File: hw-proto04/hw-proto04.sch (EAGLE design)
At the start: 35 parts, among them IC1 VN5E160MSTR-E, IC2 UCC27523DR, IC3 MCP2562T, IC4 STM32F042C6T7, IC5 TLV74333PDBVR, J1 10, J2 10, Q1 SQJ147ELP-T1_GE3, Q2 SQJ147ELP-T1_GE3

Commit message: schematic refinements
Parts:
- removed SER: (no value), SparkFun-Connectors:M04LOCK
- added UART1: (no value), SparkFun-Connectors:M04LOCK
- IC4: value STM32F042C6T7 -> STM32F042
- IC5: value TLV74333PDBVR -> TLV74333P
- renumbered J1 to R3, J2 to R2, PRG to SWLINK
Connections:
- net +3V3: now also UART1.1; no longer SER.4
- net GND: now also SWLINK.2, UART1.2; no longer SER.1, SWLINK.4
- net RX1: now also UART1.4; no longer SER.3
- net SWCLK: now also SWLINK.4; no longer SWLINK.3
- net SWDIO: now also SWLINK.3; no longer SWLINK.2
- net TX1: now also UART1.3; no longer SER.2
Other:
- moved on the sheet: PWR

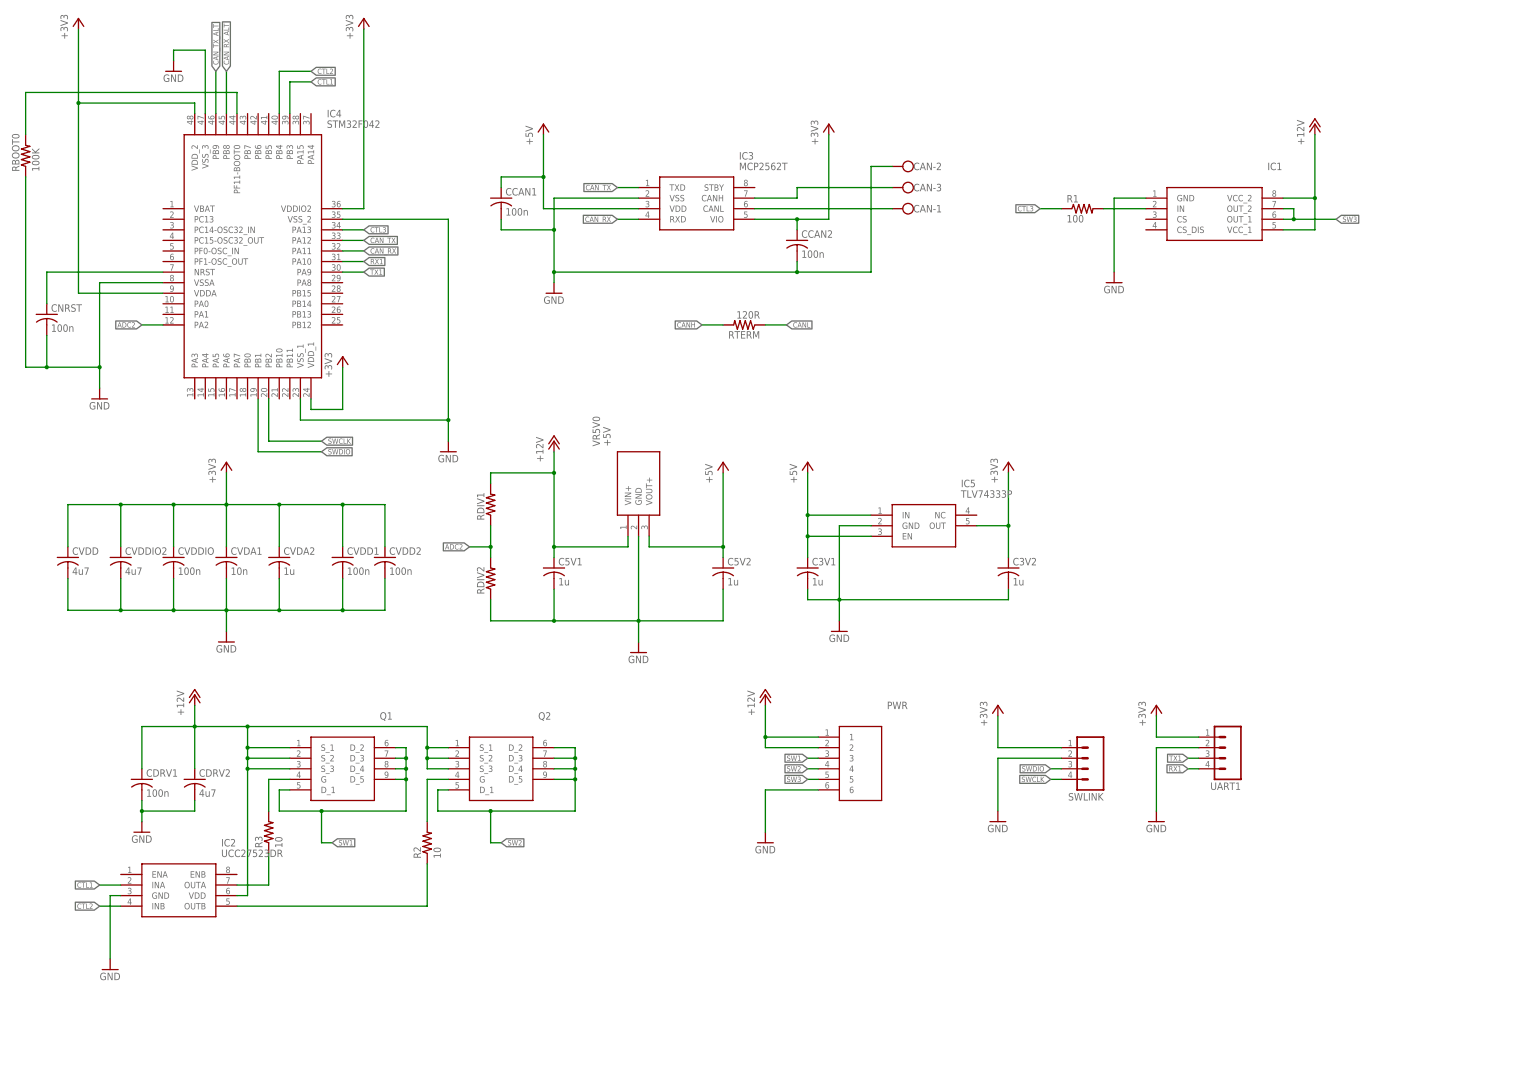
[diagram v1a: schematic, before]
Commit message: silkscreen refinement
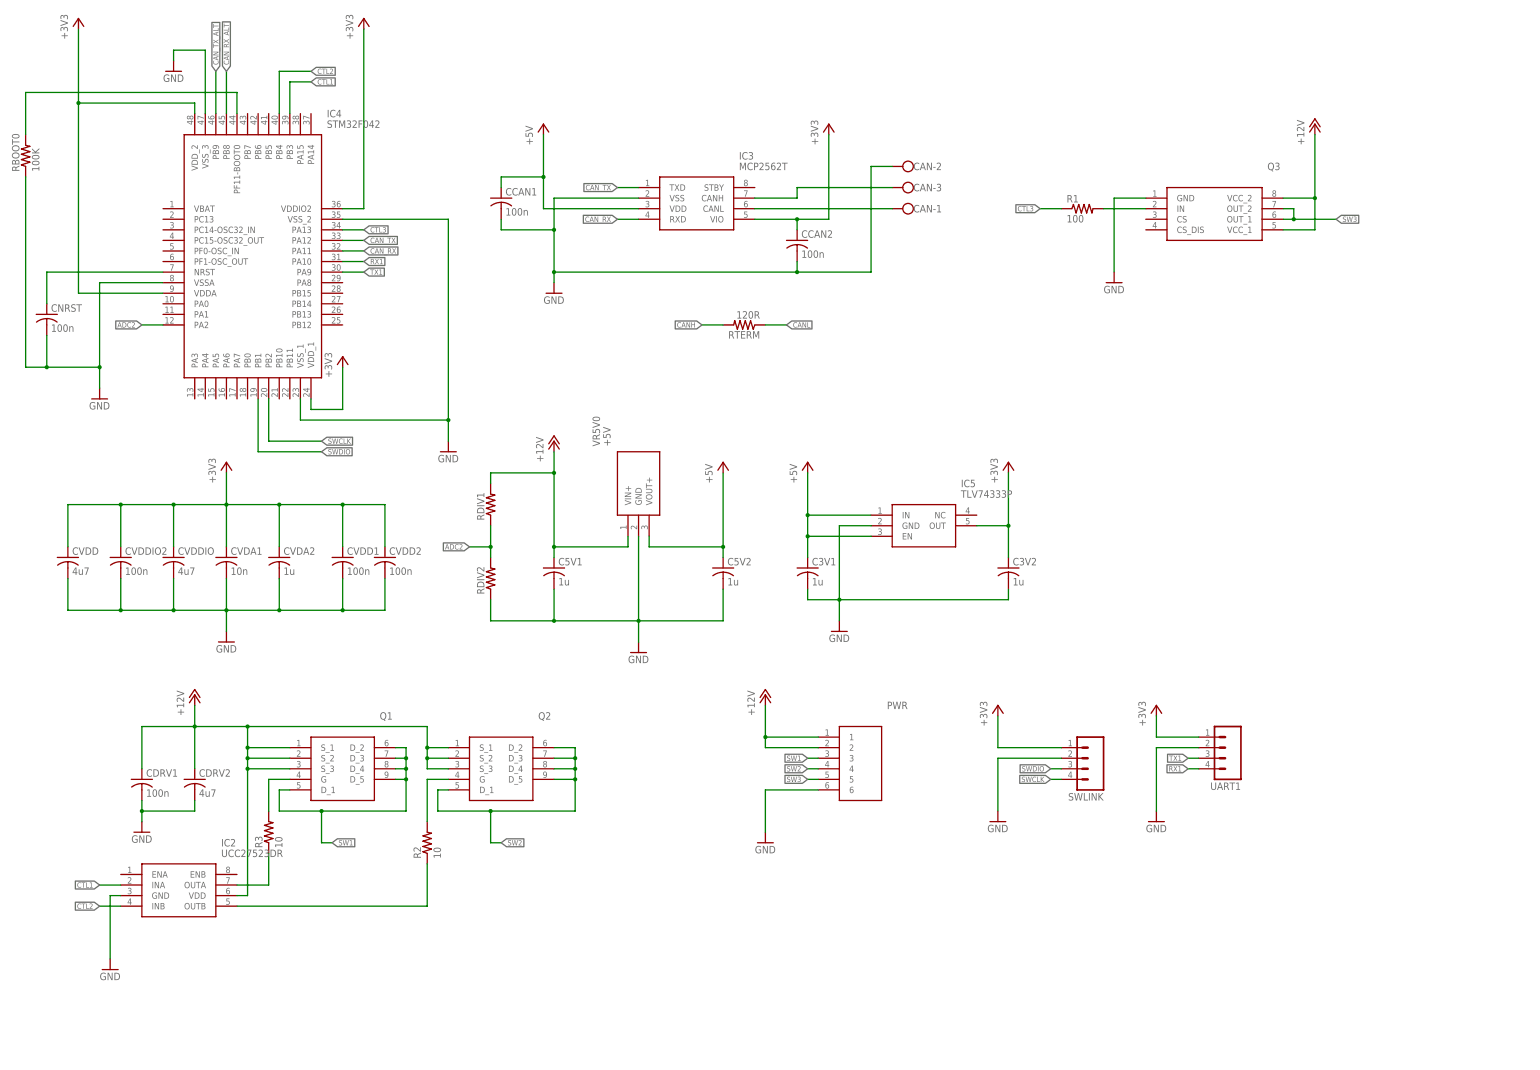
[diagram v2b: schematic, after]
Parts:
- CVDDIO: value 100n -> 4u7
- CVDDIO2: value 4u7 -> 100n
- renumbered IC1 to Q3
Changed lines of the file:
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@@
 </classes>
 <parts>
-<part name="IC1" library="VN5E160MSTR-E" deviceset="VN5E160MSTR-E" device="" value=""/>
+<part name="Q3" library="VN5E160MSTR-E" deviceset="VN5E160MSTR-E" device="" value=""/>
 <part name="IC3" library="MCP2562T-H_SN" deviceset="MCP2562T-H_SN" device="" value="MCP2562T"/>
 <part name="PWR" library="4DB-P108-06" deviceset="4DB-P108-06" device="" value=""/>
@@
 <part name="CVDD1" library="rcl" deviceset="C-US" device="C0603K" value="100n"/>
 <part name="CVDA1" library="rcl" deviceset="C-US" device="C0603K" value="10n"/>
-<part name="CVDDIO2" library="rcl" deviceset="C-US" device="C0603K" value="4u7"/>
+<part name="CVDDIO2" library="rcl" deviceset="C-US" device="C0603K" value="100n"/>
 <part name="+3V7" library="supply1" deviceset="+3V3" device=""/>
 <part name="CVDD" library="rcl" deviceset="C-US" device="C0603K" value="4u7"/>
 <part name="CVDA2" library="rcl" deviceset="C-US" device="C0603K" value="1u"/>
-<part name="CVDDIO" library="rcl" deviceset="C-US" device="C0603K" value="100n"/>
+<part name="CVDDIO" library="rcl" deviceset="C-US" device="C0603K" value="4u7"/>
 <part name="GND13" library="supply1" deviceset="GND" device=""/>
 <part name="GND5" library="supply1" deviceset="GND" device=""/>
@@
 </plain>
 <instances>
-<instance part="IC1" gate="G$1" x="218.44" y="213.36"/>
+<instance part="Q3" gate="G$1" x="218.44" y="213.36"/>
 <instance part="IC3" gate="G$1" x="96.52" y="215.9"/>
 <instance part="PWR" gate="G$1" x="139.7" y="83.82"/>
@@
 <net name="SW3" class="0">
 <segment>
-<pinref part="IC1" gate="G$1" pin="OUT_1"/>
+<pinref part="Q3" gate="G$1" pin="OUT_1"/>
 <wire x1="251.46" y1="208.28" x2="254" y2="208.28" width="0.1524" layer="91"/>
 <wire x1="254" y1="208.28" x2="264.16" y2="208.28" width="0.1524" layer="91"/>
-<pinref part="IC1" gate="G$1" pin="OUT_2"/>
+<pinref part="Q3" gate="G$1" pin="OUT_2"/>
 <wire x1="251.46" y1="210.82" x2="254" y2="210.82" width="0.1524" layer="91"/>
 <wire x1="254" y1="210.82" x2="254" y2="208.28" width="0.1524" layer="91"/>
@@
 </segment>
 <segment>
-<pinref part="IC1" gate="G$1" pin="GND"/>
+<pinref part="Q3" gate="G$1" pin="GND"/>
 <pinref part="GND2" gate="1" pin="GND"/>
 <wire x1="218.44" y1="213.36" x2="210.82" y2="213.36" width="0.1524" layer="91"/>
@@
 </segment>
 <segment>
-<pinref part="IC1" gate="G$1" pin="VCC_1"/>
+<pinref part="Q3" gate="G$1" pin="VCC_1"/>
 <pinref part="P+7" gate="1" pin="+12V"/>
 <wire x1="251.46" y1="205.74" x2="259.08" y2="205.74" width="0.1524" layer="91"/>
 <wire x1="259.08" y1="205.74" x2="259.08" y2="213.36" width="0.1524" layer="91"/>
-<pinref part="IC1" gate="G$1" pin="VCC_2"/>
+<pinref part="Q3" gate="G$1" pin="VCC_2"/>
 <wire x1="259.08" y1="213.36" x2="259.08" y2="228.6" width="0.1524" layer="91"/>
 <wire x1="251.46" y1="213.36" x2="259.08" y2="213.36" width="0.1524" layer="91"/>
@@
 <segment>
 <pinref part="R1" gate="G$1" pin="2"/>
-<pinref part="IC1" gate="G$1" pin="IN"/>
+<pinref part="Q3" gate="G$1" pin="IN"/>
 <wire x1="208.28" y1="210.82" x2="218.44" y2="210.82" width="0.1524" layer="91"/>
 </segment>

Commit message: Updated documentation for hw-proto04
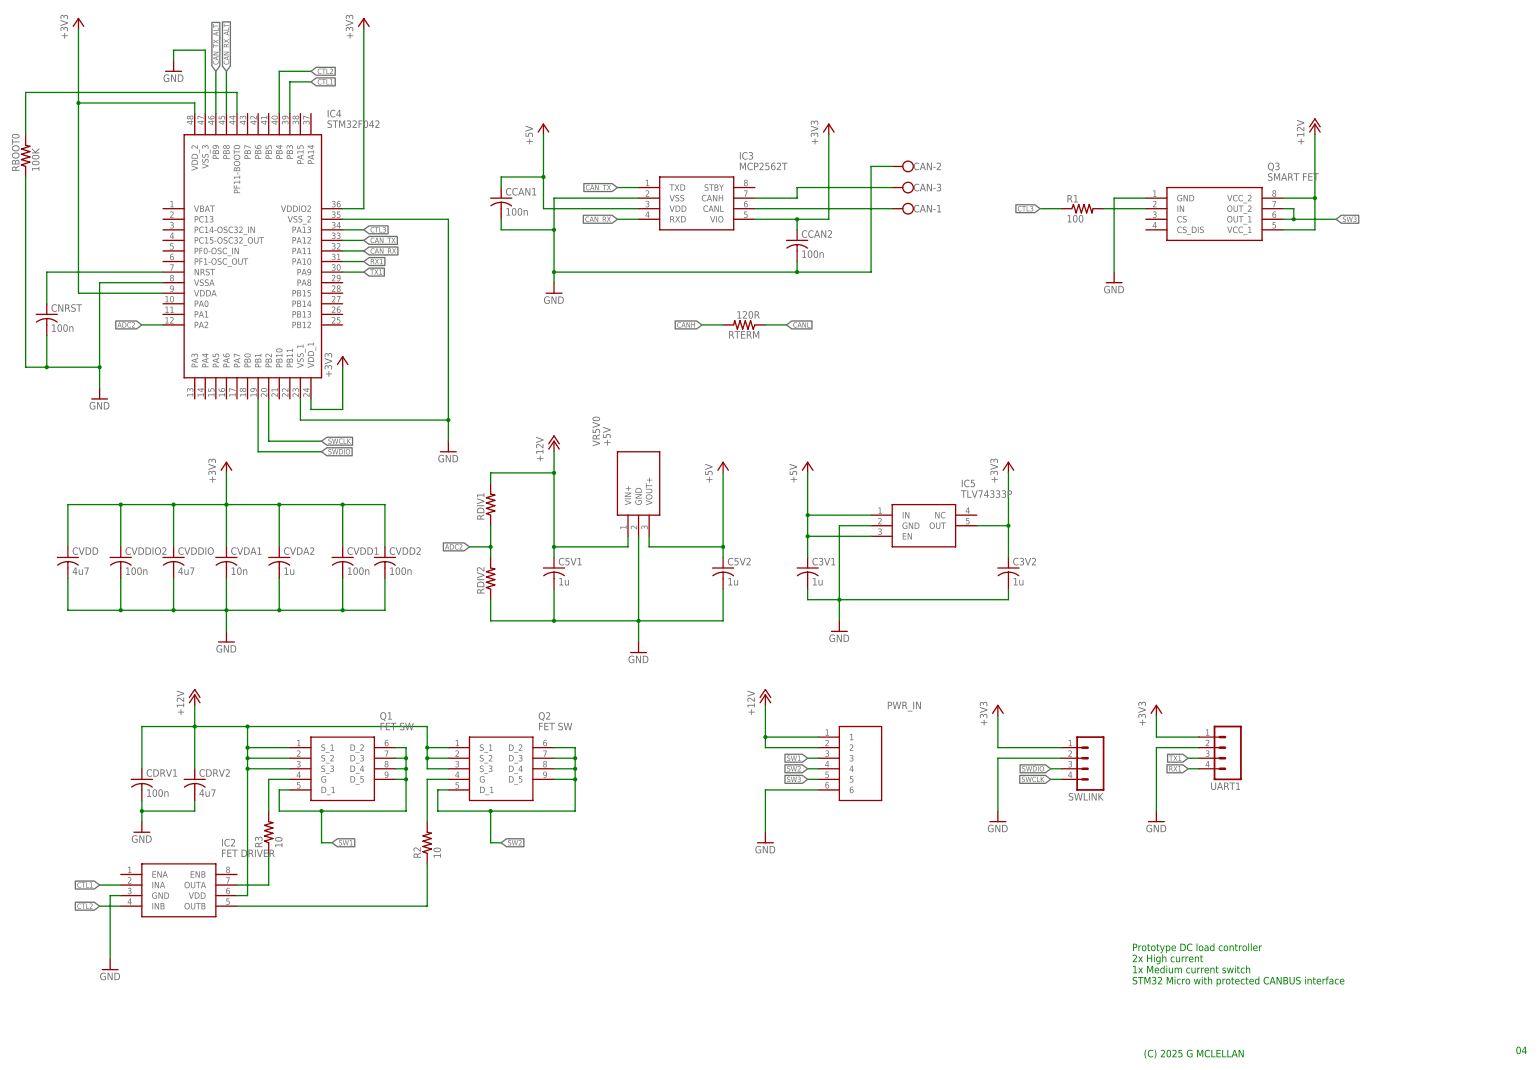
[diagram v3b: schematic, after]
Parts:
- IC2: value UCC27523DR -> FET DRIVER
- Q1, Q2: value SQJ147ELP-T1_GE3 -> FET SW
- Q3: value VN5E160MSTR-E -> SMART FET
- renumbered PWR to PWR_IN
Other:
- note added: "(C) 2025 G MCLELLAN"
- note added: "04"
- note added: "Prototype DC load controller 2x High current 1x Medium current switch STM32 Micro with protected CANBUS interface"
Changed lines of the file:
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@@
 </classes>
 <parts>
-<part name="Q3" library="VN5E160MSTR-E" deviceset="VN5E160MSTR-E" device="" value=""/>
+<part name="Q3" library="VN5E160MSTR-E" deviceset="VN5E160MSTR-E" device="" value="SMART FET"/>
 <part name="IC3" library="MCP2562T-H_SN" deviceset="MCP2562T-H_SN" device="" value="MCP2562T"/>
-<part name="PWR" library="4DB-P108-06" deviceset="4DB-P108-06" device="" value=""/>
+<part name="PWR_IN" library="4DB-P108-06" deviceset="4DB-P108-06" device="" value=""/>
 <part name="GND1" library="supply1" deviceset="GND" device=""/>
 <part name="GND2" library="supply1" deviceset="GND" device=""/>
@@
 <part name="CCAN2" library="rcl" deviceset="C-US" device="C0603K" value="100n"/>
 <part name="GND11" library="supply1" deviceset="GND" device=""/>
-<part name="Q1" library="transistor-vishay-pchan-pso8" deviceset="SQJ147ELP-T1_GE3" device="" value=""/>
-<part name="Q2" library="transistor-vishay-pchan-pso8" deviceset="SQJ147ELP-T1_GE3" device="" value=""/>
+<part name="Q1" library="transistor-vishay-pchan-pso8" deviceset="SQJ147ELP-T1_GE3" device="" value="FET SW"/>
+<part name="Q2" library="transistor-vishay-pchan-pso8" deviceset="SQJ147ELP-T1_GE3" device="" value="FET SW"/>
 <part name="CVDD2" library="rcl" deviceset="C-US" device="C0603K" value="100n"/>
 <part name="CNRST" library="rcl" deviceset="C-US" device="C0603K" value="100n"/>
-<part name="IC2" library="UCC27523DR-fet-driver" deviceset="UCC27523DR" device=""/>
+<part name="IC2" library="UCC27523DR-fet-driver" deviceset="UCC27523DR" device="" value="FET DRIVER"/>
 <part name="CDRV2" library="rcl" deviceset="C-US" device="C0805K" value="4u7"/>
 <part name="CDRV1" library="rcl" deviceset="C-US" device="C0603K" value="100n"/>
@@
 <part name="RBOOT0" library="rcl" deviceset="R-US_" device="R0603" value="100K"/>
 <part name="RTERM" library="rcl" deviceset="R-US_" device="R0805" value="120R"/>
+<part name="FRAME1" library="frames" deviceset="FRAME_B_L" device=""/>
 </parts>
 <sheets>
 <sheet>
 <plain>
+<text x="215.138" y="24.384" size="1.778" layer="91" font="vector" ratio="12">Prototype DC load controller
+2x High current
+1x Medium current switch
+STM32 Micro with protected CANBUS interface</text>
+<text x="307.34" y="7.62" size="1.778" layer="91" font="vector" ratio="12">04</text>
+<text x="217.932" y="6.858" size="1.778" layer="91" font="vector" ratio="12">(C) 2025 G MCLELLAN</text>
 </plain>
 <instances>
 <instance part="Q3" gate="G$1" x="218.44" y="213.36"/>
 <instance part="IC3" gate="G$1" x="96.52" y="215.9"/>
-<instance part="PWR" gate="G$1" x="139.7" y="83.82"/>
+<instance part="PWR_IN" gate="G$1" x="139.7" y="83.82"/>
 <instance part="GND1" gate="1" x="50.8" y="152.4"/>
 <instance part="GND2" gate="1" x="210.82" y="193.04"/>
@@
 <instance part="RBOOT0" gate="G$1" x="-50.8" y="223.52" rot="R90"/>
 <instance part="RTERM" gate="G$1" x="121.92" y="182.88" rot="R180"/>
+<instance part="FRAME1" gate="G$1" x="-111.76" y="0"/>
+<instance part="FRAME1" gate="G$2" x="213.36" y="0"/>
 </instances>
 <busses>
@@
 </segment>
 <segment>
-<pinref part="PWR" gate="G$1" pin="5"/>
+<pinref part="PWR_IN" gate="G$1" pin="5"/>
 <wire x1="137.16" y1="73.66" x2="139.7" y2="73.66" width="0.1524" layer="91"/>
 <label x="137.16" y="73.66" size="1.27" layer="95" rot="R180" xref="yes"/>
@@
 <pinref part="GND4" gate="1" pin="GND"/>
 <wire x1="127" y1="71.12" x2="127" y2="60.96" width="0.1524" layer="91"/>
-<pinref part="PWR" gate="G$1" pin="6"/>
+<pinref part="PWR_IN" gate="G$1" pin="6"/>
 <wire x1="139.7" y1="71.12" x2="127" y2="71.12" width="0.1524" layer="91"/>
 </segment>
@@
 </segment>
 <segment>
-<pinref part="PWR" gate="G$1" pin="3"/>
+<pinref part="PWR_IN" gate="G$1" pin="3"/>
 <wire x1="137.16" y1="78.74" x2="139.7" y2="78.74" width="0.1524" layer="91"/>
 <label x="137.16" y="78.74" size="1.27" layer="95" rot="R180" xref="yes"/>
@@
 </segment>
 <segment>
-<pinref part="PWR" gate="G$1" pin="4"/>
+<pinref part="PWR_IN" gate="G$1" pin="4"/>
 <wire x1="137.16" y1="76.2" x2="139.7" y2="76.2" width="0.1524" layer="91"/>
 <label x="137.16" y="76.2" size="1.27" layer="95" rot="R180" xref="yes"/>
@@
 </segment>
 <segment>
-<pinref part="PWR" gate="G$1" pin="1"/>
+<pinref part="PWR_IN" gate="G$1" pin="1"/>
 <wire x1="139.7" y1="83.82" x2="127" y2="83.82" width="0.1524" layer="91"/>
 <wire x1="127" y1="83.82" x2="127" y2="91.44" width="0.1524" layer="91"/>
 <pinref part="P+2" gate="1" pin="+12V"/>
-<pinref part="PWR" gate="G$1" pin="2"/>
+<pinref part="PWR_IN" gate="G$1" pin="2"/>
 <wire x1="139.7" y1="81.28" x2="127" y2="81.28" width="0.1524" layer="91"/>
 <wire x1="127" y1="81.28" x2="127" y2="83.82" width="0.1524" layer="91"/>
@@
 </schematic>
 </drawing>
+<compatibility>
+<note version="6.3" minversion="6.2.2" severity="warning">
+Since Version 6.2.2 text objects can contain more than one line,
+which will not be processed correctly with this version.
+</note>
+</compatibility>
 </eagle>
